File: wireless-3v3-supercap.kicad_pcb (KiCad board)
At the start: 2 copper layers, 88 x 40 mm, 20 parts

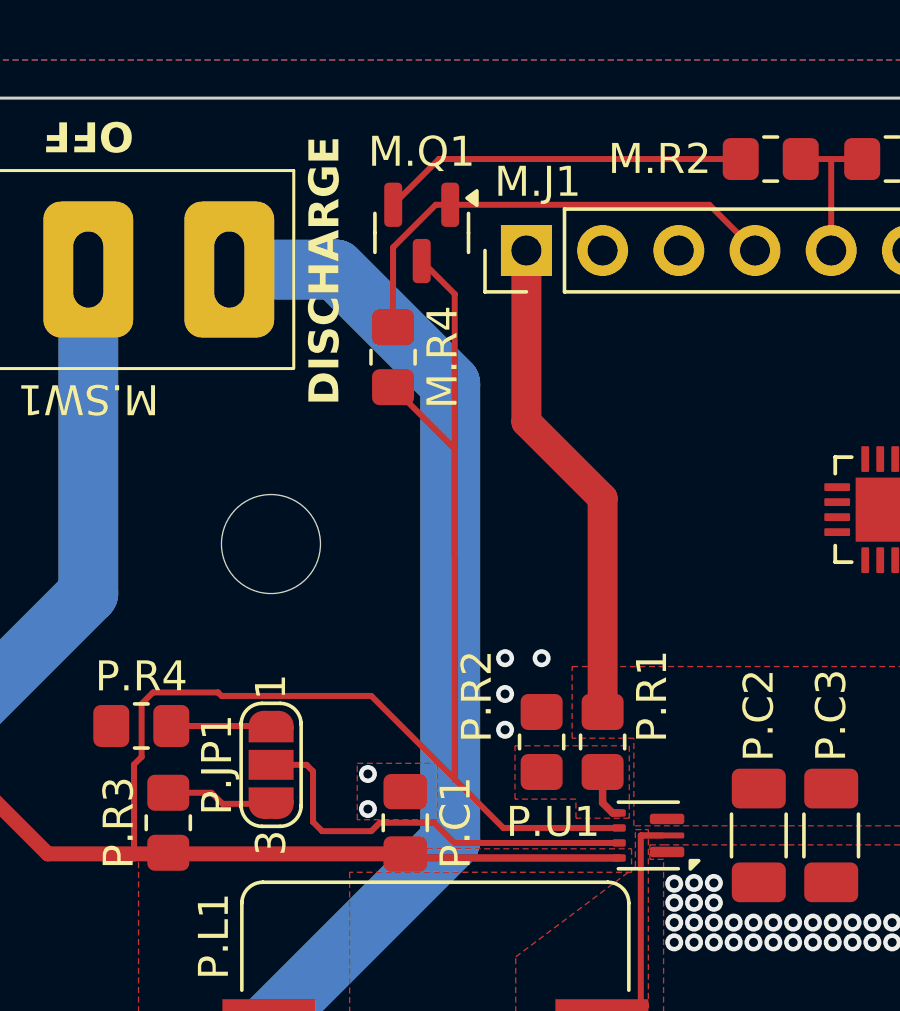
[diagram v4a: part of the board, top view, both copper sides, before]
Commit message: Fix MOSFET for measuring capacitor voltage
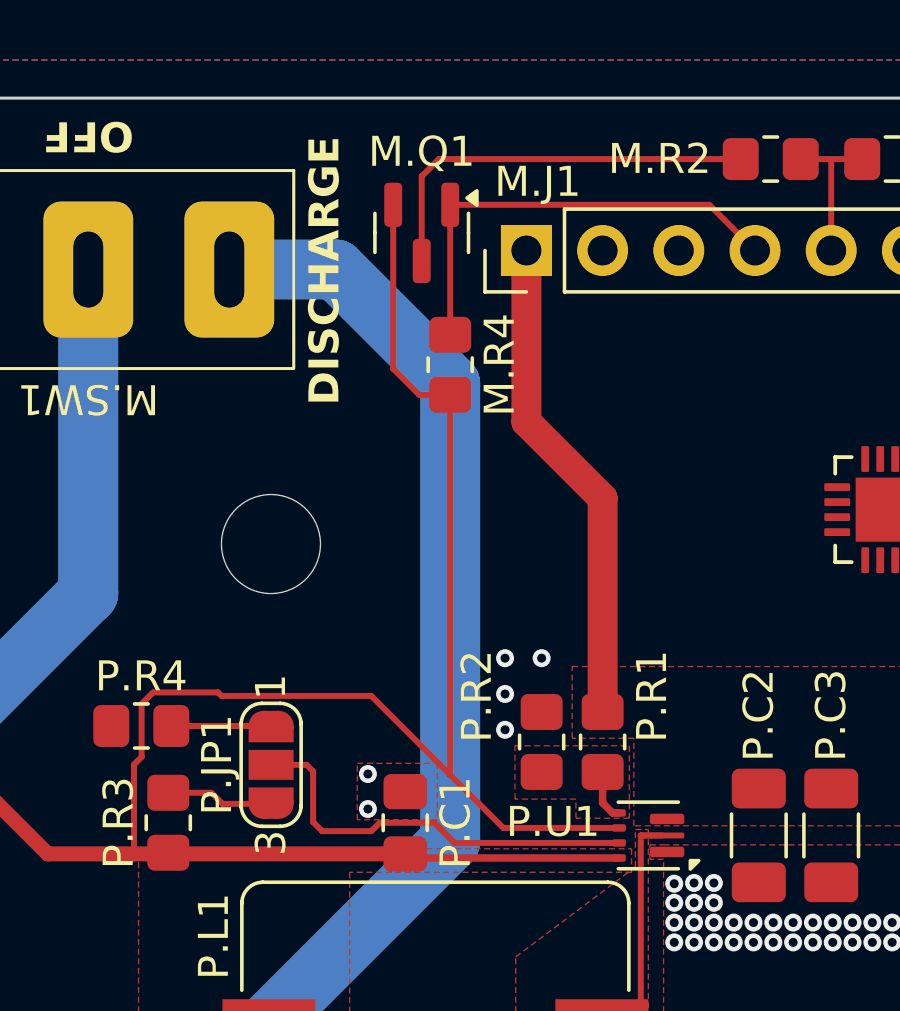
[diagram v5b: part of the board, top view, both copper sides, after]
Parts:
- moved M.R4 1.92 mm to (81.3, 34.3)
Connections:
- M.Q1 pad 2: Net-(M.Q1-S) -> /Charge/SUPERCAP
- M.Q1 pad 3: /Charge/SUPERCAP -> Net-(M.Q1-D)
- M.R2 pad 1: Net-(M.Q1-S) -> Net-(M.Q1-D)
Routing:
- net Net-(M.Q1-D): track 0.00 -> 14.7 mm
- net Net-(M.Q1-S): track 13.2 -> 0.00 mm
- net /Charge/SUPERCAP: track 87.0 -> 83.2 mm
- net MEASURE_VOLTAGE: track 15.9 -> 15.1 mm
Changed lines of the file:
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@@
 	(net 28 "unconnected-(C.TH1-Pad1)")
 	(net 29 "MEASURE_VOLTAGE")
-	(net 30 "Net-(M.Q1-S)")
+	(net 30 "Net-(M.Q1-D)")
 	(footprint "Resistor_SMD:R_0805_2012Metric_Pad1.20x1.40mm_HandSolder"
 		(layer "F.Cu")
-		(at 79.375 34.036 -90)
+		(at 81.28 34.29 -90)
 		(descr "Resistor SMD 0805 (2012 Metric), square (rectangular) end terminal, IPC-7351 nominal with elongated pad for handsoldering. (Body size source: IPC-SM-782 page 72, https://www.pcb-3d.com/wordpress/wp-content/uploads/ipc-sm-782a_amendment_1_and_2.pdf), generated with kicad-footprint-generator")
 		(tags "resistor handsolder")
@@
 		(attr smd)
 		(fp_line
-			(start -0.227065 0.735)
-			(end 0.227064 0.735)
+			(start -0.227064 -0.735)
+			(end 0.227064 -0.735)
 			(stroke
 				(width 0.12)
@@
 		)
 		(fp_line
-			(start -0.227064 -0.735)
-			(end 0.227065 -0.735)
+			(start -0.227064 0.735)
+			(end 0.227064 0.735)
 			(stroke
 				(width 0.12)
@@
 		)
 		(fp_line
-			(start -1.850001 0.95)
-			(end -1.85 -0.95)
+			(start -1.85 -0.95)
+			(end 1.85 -0.95)
 			(stroke
 				(width 0.05)
@@
 		)
 		(fp_line
-			(start -1.85 -0.95)
-			(end 1.850001 -0.95)
+			(start -1.85 0.95)
+			(end -1.85 -0.95)
 			(stroke
 				(width 0.05)
@@
 		)
 		(fp_line
-			(start 1.85 0.95)
-			(end -1.850001 0.95)
+			(start 1.85 -0.95)
+			(end 1.85 0.95)
 			(stroke
 				(width 0.05)
@@
 		)
 		(fp_line
-			(start 1.850001 -0.95)
-			(end 1.85 0.95)
+			(start 1.85 0.95)
+			(end -1.85 0.95)
 			(stroke
 				(width 0.05)
@@
 		)
 		(pad "1" smd roundrect
-			(at -1.000001 0)
+			(at -1 0)
 			(size 1.2 1.4)
 			(layers "F.Cu" "F.Mask" "F.Paste")
 			(roundrect_rratio 0.208333)
-			(net 30 "Net-(M.Q1-S)")
+			(net 30 "Net-(M.Q1-D)")
 			(pintype "passive")
 		)
 		(pad "2" smd roundrect
-			(at 1.000001 0)
+			(at 1 0)
 			(size 1.2 1.4)
 			(layers "F.Cu" "F.Mask" "F.Paste")
@@
 		(tags "SOT TO_SOT_SMD")
 		(property "Reference" "M.Q1"
-			(at -2.7 0 180)
+			(at -2.7 0 0)
 			(layer "F.SilkS")
 			(effects
@@
 		)
 		(property "Value" "DMP2004K"
-			(at 0 2.4 90)
+			(at 0 2.4 270)
 			(layer "F.Fab")
 			(effects
@@
 		)
 		(property "Datasheet" "https://www.diodes.com/assets/Datasheets/DMP2004K.pdf"
-			(at 0 0 90)
+			(at 0 0 270)
 			(layer "F.Fab")
 			(hide yes)
@@
 		)
 		(property "Description" "P-MOSFET transistor, drain/source/gate"
-			(at 0 0 90)
+			(at 0 0 270)
 			(layer "F.Fab")
 			(hide yes)
@@
 		)
 		(fp_text user "${REFERENCE}"
-			(at 0 0 90)
+			(at 0 0 270)
 			(layer "F.Fab")
 			(effects
@@
 			(layers "F.Cu" "F.Mask" "F.Paste")
 			(roundrect_rratio 0.25)
-			(net 30 "Net-(M.Q1-S)")
+			(net 7 "/Charge/SUPERCAP")
 			(pinfunction "S")
 			(pintype "passive")
@@
 			(layers "F.Cu" "F.Mask" "F.Paste")
 			(roundrect_rratio 0.25)
-			(net 7 "/Charge/SUPERCAP")
+			(net 30 "Net-(M.Q1-D)")
 			(pinfunction "D")
 			(pintype "passive")
@@
 	)
 	(segment
-		(start 81.43104 31.93204)
-		(end 81.43104 40.64)
-		(width 0.2)
-		(layer "F.Cu")
-		(net 7)
-	)
-	(segment
 		(start 71.374 45.212)
 		(end 70.993 45.593)
@@
 	)
 	(segment
-		(start 80.33 30.831)
-		(end 81.43104 31.93204)
-		(width 0.2)
-		(layer "F.Cu")
-		(net 7)
-	)
-	(segment
 		(start 78.65068 45.3286)
 		(end 73.66 45.3286)
@@
 	)
 	(segment
-		(start 79.375 35.036)
-		(end 81.43104 37.09204)
+		(start 80.248 35.29)
+		(end 81.28 35.29)
 		(width 0.2)
 		(layer "F.Cu")
@@
 	)
 	(segment
-		(start 81.43104 37.09204)
-		(end 81.43104 40.64)
-		(width 0.2)
-		(layer "F.Cu")
-		(net 7)
-	)
-	(segment
 		(start 64.515 31.115)
 		(end 64.515 46.228)
@@
 	)
 	(segment
-		(start 73.66 45.3286)
-		(end 73.5434 45.212)
+		(start 79.38 28.956)
+		(end 79.38 34.422)
 		(width 0.2)
 		(layer "F.Cu")
@@
 	)
 	(segment
-		(start 78.65068 45.3286)
-		(end 81.43104 48.10896)
+		(start 73.66 45.3286)
+		(end 73.5434 45.212)
 		(width 0.2)
 		(layer "F.Cu")
@@
 	)
 	(segment
+		(start 79.38 34.422)
+		(end 80.248 35.29)
+		(width 0.2)
+		(layer "F.Cu")
+		(net 7)
+	)
+	(segment
 		(start 70.739 50.5929)
 		(end 67.8649 50.5929)
@@
 	)
 	(segment
-		(start 81.43104 48.10896)
+		(start 78.65068 45.3286)
 		(end 83.05048 49.7284)
 		(width 0.2)
@@
 	)
 	(segment
-		(start 81.43104 40.64)
-		(end 81.43104 48.10896)
-		(width 0.2)
-		(layer "F.Cu")
-		(net 7)
-	)
-	(segment
 		(start 70.993 47.36062)
 		(end 70.739 47.61462)
@@
 	)
 	(segment
+		(start 81.28 35.29)
+		(end 81.28 47.95792)
+		(width 0.2)
+		(layer "F.Cu")
+		(net 7)
+	)
+	(segment
 		(start 81.28 34.925)
 		(end 77.47 31.115)
@@
 	)
 	(segment
-		(start 80.7974 28.956)
-		(end 79.375 30.3784)
-		(width 0.2)
-		(layer "F.Cu")
-		(net 29)
-	)
-	(segment
 		(start 89.916 28.956)
 		(end 81.28 28.956)
@@
 	(segment
 		(start 81.28 28.956)
-		(end 80.7974 28.956)
+		(end 81.28 33.29)
 		(width 0.2)
 		(layer "F.Cu")
@@
 	)
 	(segment
-		(start 79.375 30.3784)
-		(end 79.375 33.036)
+		(start 80.33 28.006)
+		(end 80.904 27.432)
 		(width 0.2)
 		(layer "F.Cu")
-		(net 29)
+		(net 30)
 	)
 	(segment
@@
 	)
 	(segment
-		(start 80.904 27.432)
-		(end 79.38 28.956)
+		(start 80.33 30.831)
+		(end 80.33 28.006)
 		(width 0.2)
 		(layer "F.Cu")

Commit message: Mark signals as active low
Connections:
- M.J1 pad 2: EXTERNAL_POWER_PRESENT -> ~{EXTERNAL_POWER_PRESENT}
- M.J1 pad 4: MEASURE_VOLTAGE -> ~{MEASURE_VOLTAGE}
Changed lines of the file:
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@@
 	(net 29 "MEASURE_VOLTAGE")
 	(net 30 "Net-(M.Q1-D)")
+	(net 31 "~{MEASURE_VOLTAGE}")
+	(net 32 "~{EXTERNAL_POWER_PRESENT}")
 	(footprint "Resistor_SMD:R_0805_2012Metric_Pad1.20x1.40mm_HandSolder"
 		(layer "F.Cu")
@@
 			(layers "*.Cu" "*.Mask")
 			(remove_unused_layers no)
-			(net 5 "EXTERNAL_POWER_PRESENT")
+			(net 32 "~{EXTERNAL_POWER_PRESENT}")
 			(pinfunction "Pin_2")
 			(pintype "passive")
@@
 			(layers "*.Cu" "*.Mask")
 			(remove_unused_layers no)
-			(net 29 "MEASURE_VOLTAGE")
+			(net 31 "~{MEASURE_VOLTAGE}")
 			(pinfunction "Pin_4")
 			(pintype "passive")

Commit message: Adjust ADC voltage divider
Increase the value of the 0.5V minimum voltage reading to improve accuracy
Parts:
- M.R2: value 26.1kΩ 1% 125mW -> 20kΩ 1% 125mW
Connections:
- C.U1 pad 5: EXTERNAL_POWER_PRESENT -> ~{EXTERNAL_POWER_PRESENT}
- M.Q1 pad 1: MEASURE_VOLTAGE -> ~{MEASURE_VOLTAGE}
- M.R4 pad 1: MEASURE_VOLTAGE -> ~{MEASURE_VOLTAGE}
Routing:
- net ~{MEASURE_VOLTAGE}: track 0.00 -> 15.1 mm
- net MEASURE_VOLTAGE: track 15.1 -> 0.00 mm

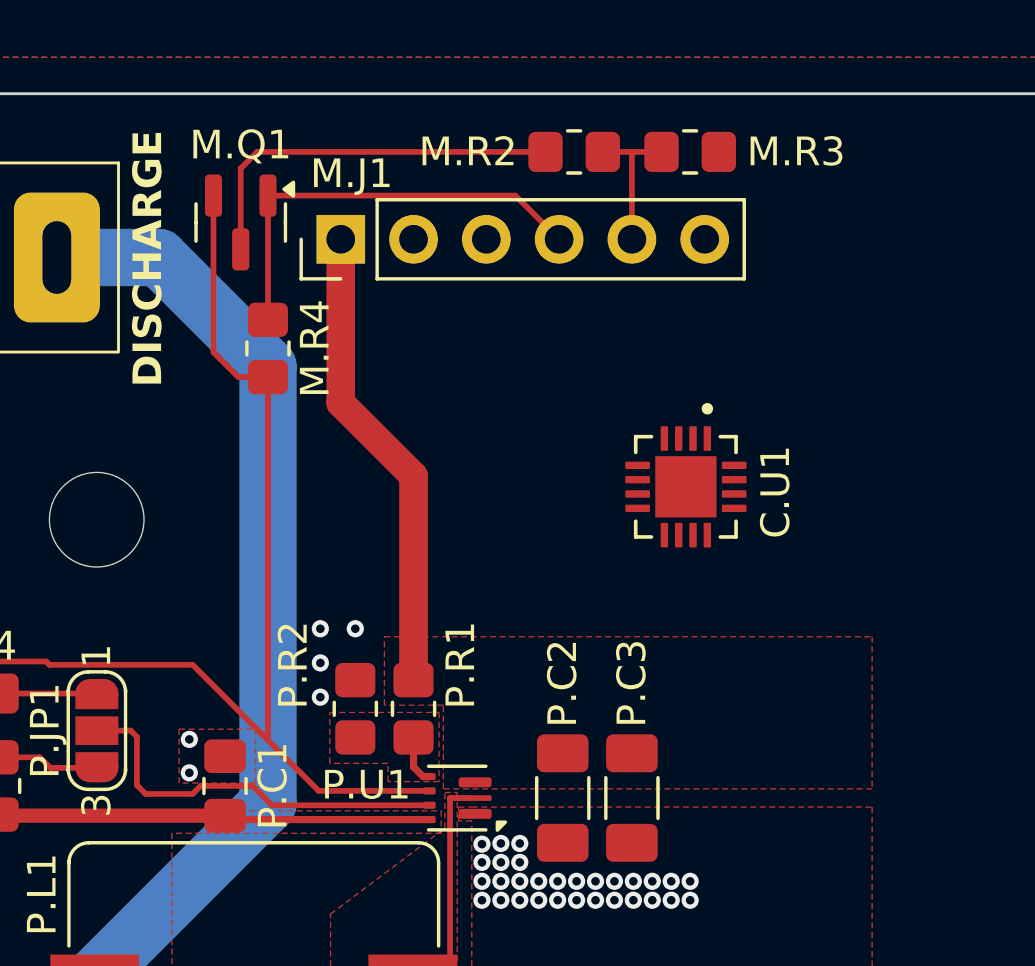
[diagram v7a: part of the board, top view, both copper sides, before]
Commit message: Remove voltage divider circuit for ADC
The ESP32-C3 can be configured to handle this directly
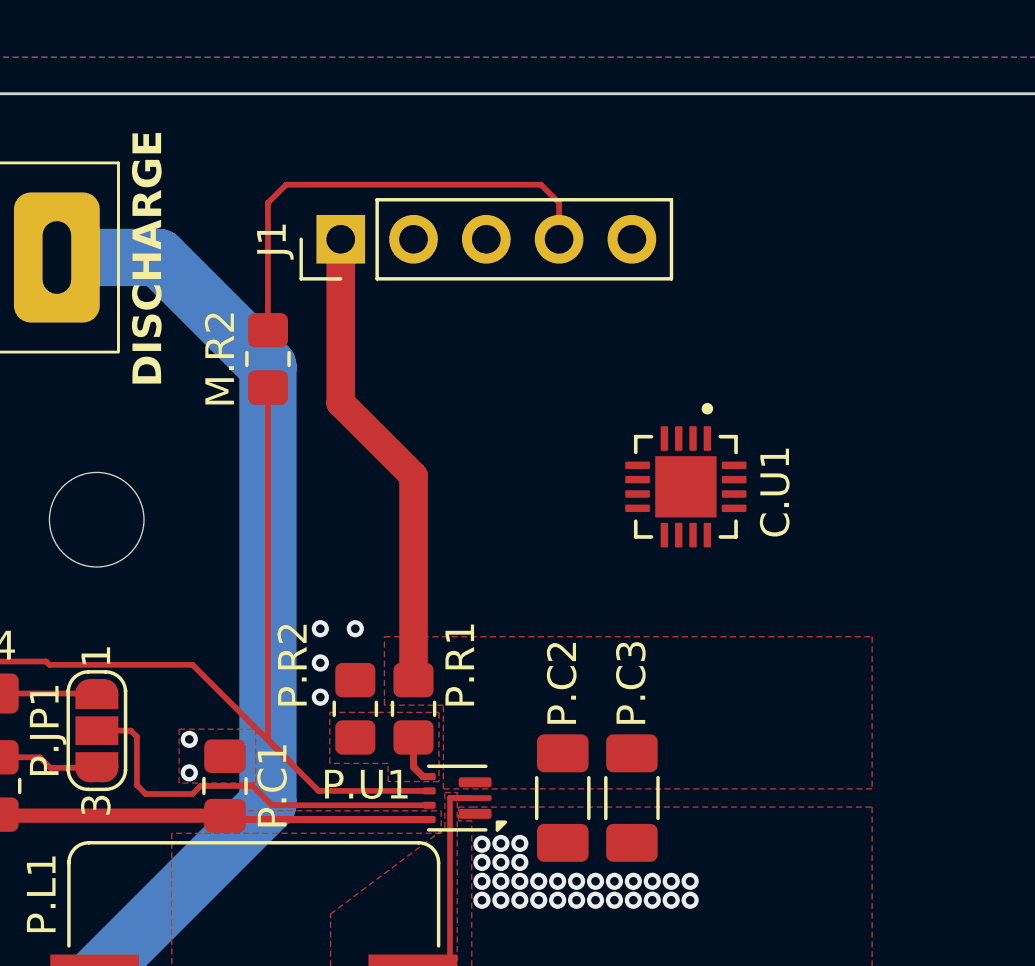
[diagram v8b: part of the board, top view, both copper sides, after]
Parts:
- removed M.Q1: DMP2004K, Package_TO_SOT_SMD:SOT-23
- removed M.R3, M.R4: 10kΩ 1% 125mW, Resistor_SMD:R_0805_2012Metric_Pad1.20x1.40mm_HandSolder
- J1: renamed from M.J1; value POWER-OUT -> Conn_01x05_Pin; footprint Connector_PinHeader_2.54mm:PinHeader_1x06_P2.54mm_Vertical -> Connector_PinHeader_2.54mm:PinHeader_1x05_P2.54mm_Vertical
- M.R2: value 20kΩ 1% 125mW -> 1kΩ 1% 125mW
- moved M.R2 12.9 mm to (81.3, 34.7), turned to 90 degrees
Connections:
- J1 pad 4: ~{MEASURE_VOLTAGE} -> CAPACITOR_VOLTAGE
- J1 pad 5: CAPACITOR_VOLTAGE -> GND
- M.R2 pad 1: Net-(M.Q1-D) -> /Charge/SUPERCAP
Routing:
- net ~{MEASURE_VOLTAGE}: track 15.1 -> 0.00 mm
- net Net-(M.Q1-D): track 14.7 -> 0.00 mm
- net CAPACITOR_VOLTAGE: track 5.10 -> 16.4 mm
- net /Charge/SUPERCAP: track 83.2 -> 76.2 mm
